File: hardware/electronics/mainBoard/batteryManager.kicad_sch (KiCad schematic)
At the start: 37 parts, among them J27 S3B-XH-SM4-TB, J28 1726480102, Q6 BUK6D72-30EX, Q7 BUK6D72-30EX, U22 BQ76905

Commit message: assigned FPs
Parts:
- D20: footprint (none) -> lib_diodes:SOD123
- J27: footprint (none) -> lib_connectors:JST_XH_S3B-SM4-TB
- J28: footprint (none) -> lib_connectors:1726480102
- Q6, Q7: footprint (none) -> lib_ICs:UDFN6P65_200X200X65L30X25N
- U22: footprint (none) -> lib_ICs:QFN50P350X350X100-20
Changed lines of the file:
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@@
 			)
 		)
-		(property "Footprint" ""
+		(property "Footprint" "lib_ICs:UDFN6P65_200X200X65L30X25N"
 			(at 186.055 142.24 90)
 			(effects
@@
 			)
 		)
-		(property "Footprint" ""
+		(property "Footprint" "lib_connectors:1726480102"
 			(at 26.67 64.77 0)
 			(effects
@@
 			)
 		)
-		(property "Footprint" ""
+		(property "Footprint" "lib_ICs:UDFN6P65_200X200X65L30X25N"
 			(at 205.105 142.24 90)
 			(effects
@@
 			)
 		)
-		(property "Footprint" ""
+		(property "Footprint" "lib_connectors:JST_XH_S3B-SM4-TB"
 			(at 35.56 30.48 0)
 			(effects
@@
 			)
 		)
-		(property "Footprint" ""
+		(property "Footprint" "lib_diodes:SOD123"
 			(at 224.79 133.35 90)
 			(effects
@@
 			)
 		)
-		(property "Footprint" ""
+		(property "Footprint" "lib_ICs:QFN50P350X350X100-20"
 			(at 154.94 99.06 0)
 			(effects

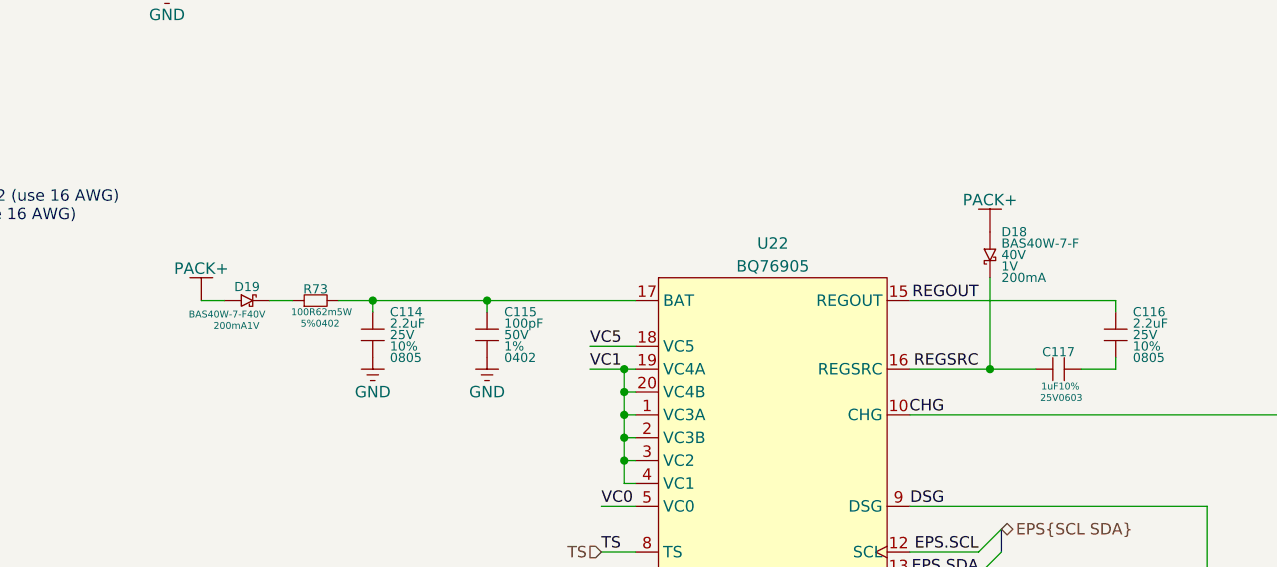
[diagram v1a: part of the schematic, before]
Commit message: added footprints to symbols
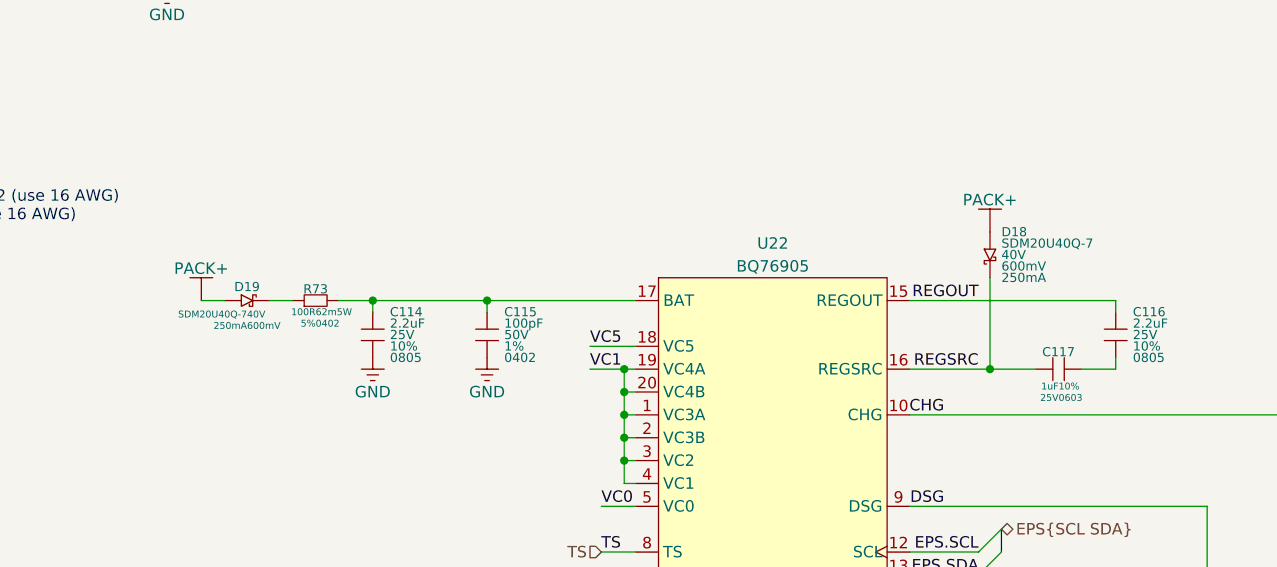
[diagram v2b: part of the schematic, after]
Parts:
- D18, D19: value BAS40W-7-F -> SDM20U40Q-7; footprint (none) -> lib_diodes:SOD523; Current 200mA -> 250mA; DKPN BAS40W-FDICT-ND -> 31-SDM20U40Q-7CT-ND; Forward Voltage 1V -> 600mV; MPN BAS40W-7-F -> SDM20U40Q-7
- R77: footprint (none) -> lib_passives:WSR4527
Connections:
- net PACK+: now also D18.2, D19.2; no longer D18.1, D19.1
- net REGSRC: now also D18.1; no longer D18.2
- net at R73.1: now also D19.1; no longer D19.2
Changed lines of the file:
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@@
 			)
 		)
-		(property "Footprint" ""
+		(property "Footprint" "lib_passives:WSR4527"
 			(at 88.9 121.92 0)
 			(effects
@@
 			)
 		)
-		(property "Value" "BAS40W-7-F"
+		(property "Value" "SDM20U40Q-7"
 			(at 165.1 81.28 0)
 			(do_not_autoplace yes)
@@
 			)
 		)
-		(property "Footprint" ""
+		(property "Footprint" "lib_diodes:SOD523"
 			(at 163.83 82.55 90)
 			(effects
@@
 			)
 		)
-		(property "Datasheet" "datasheets/Diodes-Incorporated-BAS40W_-04_-05_-06.pdf"
+		(property "Datasheet" "datasheets/Diodes-Incorporated-SDM20U40Q.pdf"
 			(at 163.83 82.55 90)
 			(effects
@@
 			)
 		)
-		(property "Description" "DIODE SCHOTTKY 40V 200MA SOT323"
+		(property "Description" "DIODE SCHOTTKY 40V 250MA SOD523"
 			(at 163.83 82.55 90)
 			(effects
@@
 			)
 		)
-		(property "MPN" "BAS40W-7-F"
+		(property "MPN" "SDM20U40Q-7"
 			(at 163.83 82.55 90)
 			(effects
@@
 			)
 		)
-		(property "DKPN" "BAS40W-FDICT-ND"
+		(property "DKPN" "31-SDM20U40Q-7CT-ND"
 			(at 163.83 82.55 90)
 			(effects
@@
 			)
 		)
-		(property "Forward Voltage" "1V"
+		(property "Forward Voltage" "600mV"
 			(at 165.1 83.82 0)
 			(do_not_autoplace yes)
@@
 			)
 		)
-		(property "Current" "200mA"
+		(property "Current" "250mA"
 			(at 165.1 85.09 0)
 			(do_not_autoplace yes)
@@
 			)
 		)
-		(property "Value" "BAS40W-7-F"
+		(property "Value" "SDM20U40Q-7"
 			(at 81.28 89.154 0)
 			(do_not_autoplace yes)
@@
 			)
 		)
-		(property "Footprint" ""
+		(property "Footprint" "lib_diodes:SOD523"
 			(at 81.28 87.63 0)
 			(effects
@@
 			)
 		)
-		(property "Datasheet" "datasheets/Diodes-Incorporated-BAS40W_-04_-05_-06.pdf"
+		(property "Datasheet" "datasheets/Diodes-Incorporated-SDM20U40Q.pdf"
 			(at 81.28 87.63 0)
 			(effects
@@
 			)
 		)
-		(property "Description" "DIODE SCHOTTKY 40V 200MA SOT323"
+		(property "Description" "DIODE SCHOTTKY 40V 250MA SOD523"
 			(at 81.28 87.63 0)
 			(effects
@@
 			)
 		)
-		(property "MPN" "BAS40W-7-F"
+		(property "MPN" "SDM20U40Q-7"
 			(at 81.28 87.63 0)
 			(effects
@@
 			)
 		)
-		(property "DKPN" "BAS40W-FDICT-ND"
+		(property "DKPN" "31-SDM20U40Q-7CT-ND"
 			(at 81.28 87.63 0)
 			(effects
@@
 			)
 		)
-		(property "Forward Voltage" "1V"
+		(property "Forward Voltage" "600mV"
 			(at 81.28 90.424 0)
 			(do_not_autoplace yes)
@@
 			)
 		)
-		(property "Current" "200mA"
+		(property "Current" "250mA"
 			(at 81.28 90.424 0)
 			(do_not_autoplace yes)

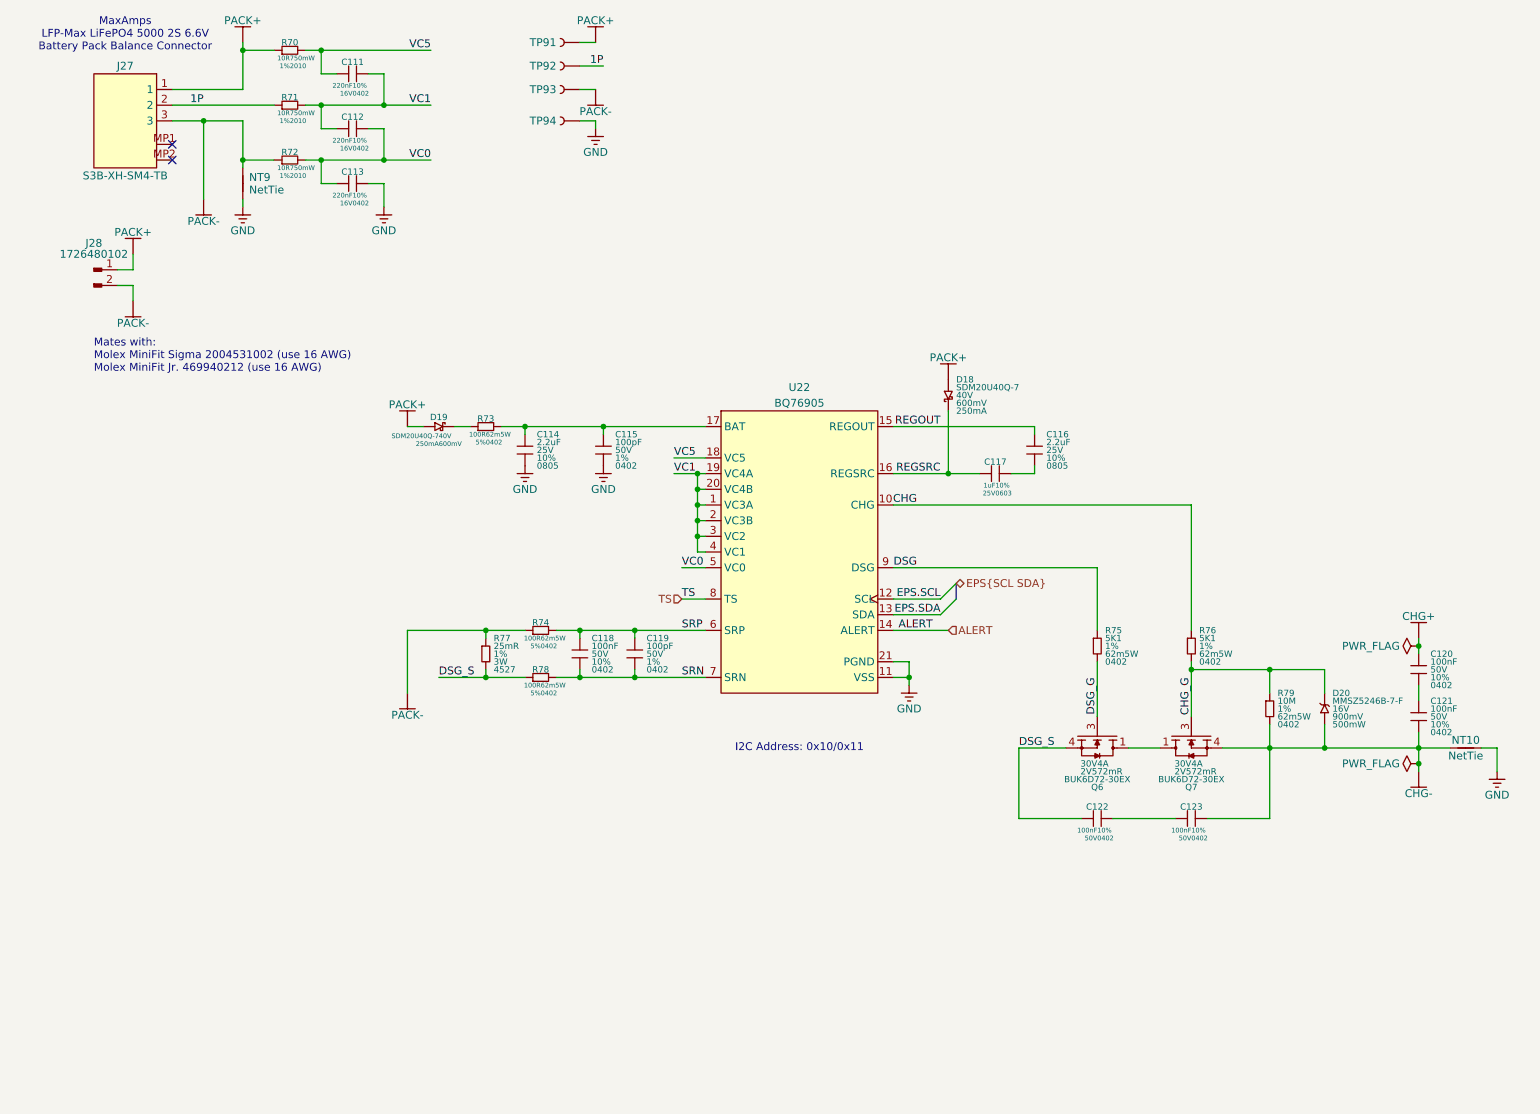
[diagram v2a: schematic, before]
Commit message: assigned footprints
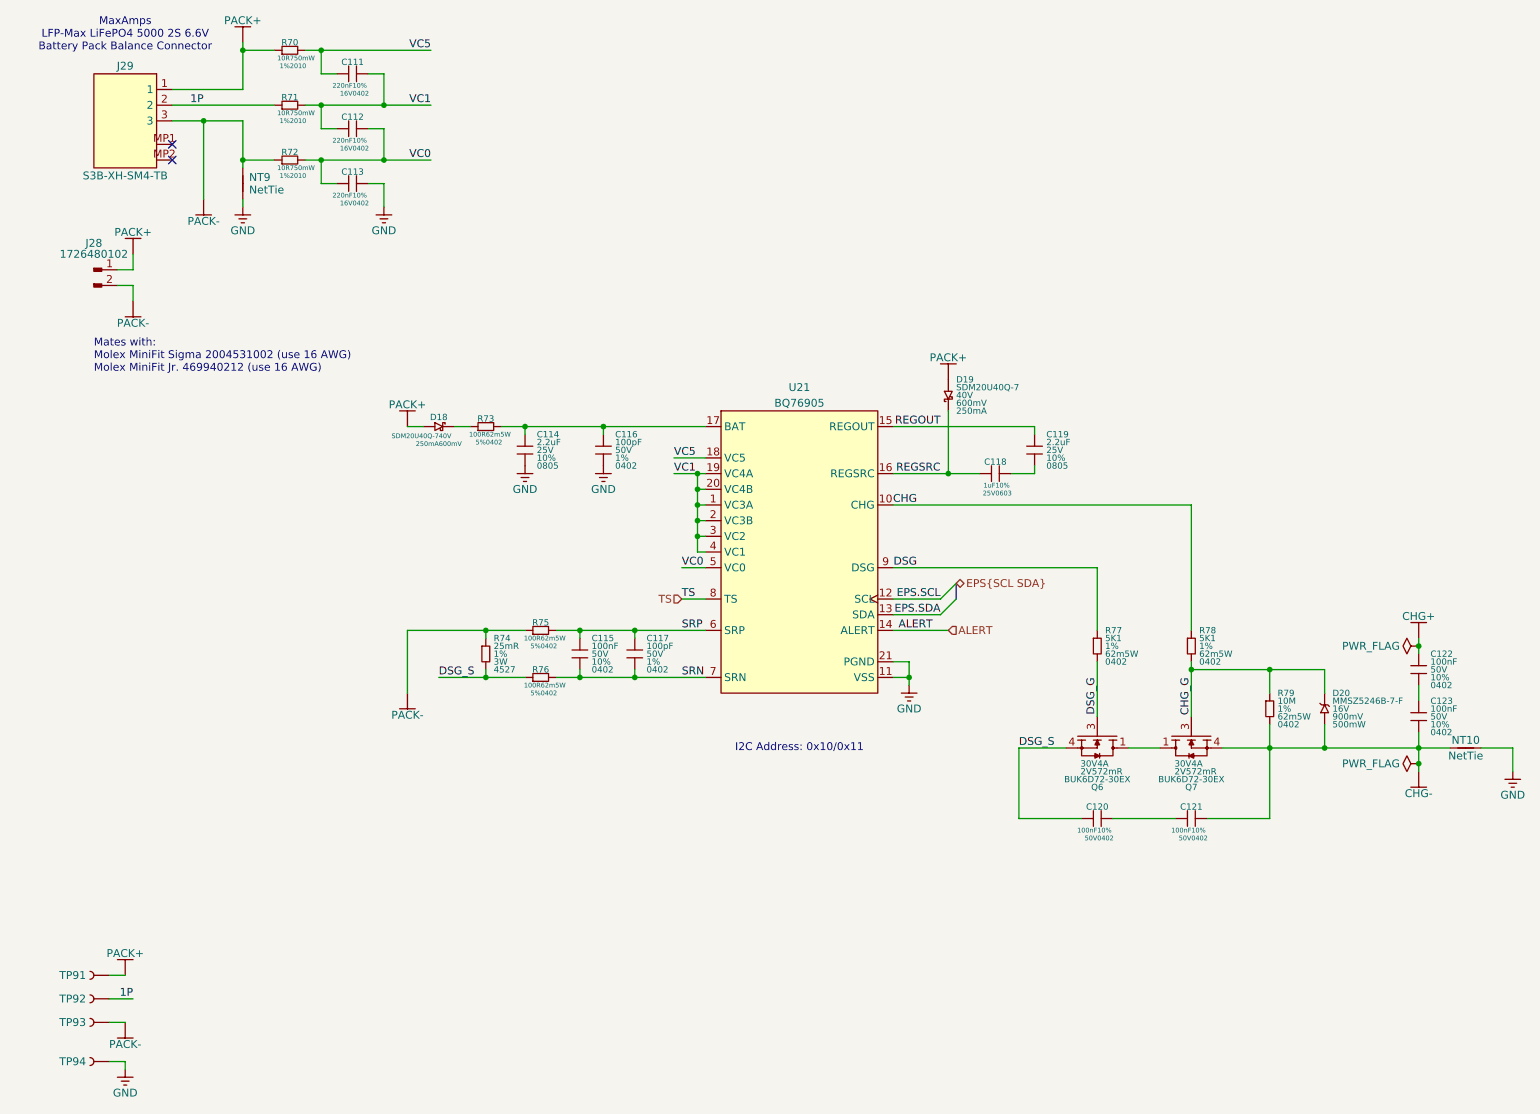
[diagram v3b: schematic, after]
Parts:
- C111, C112, C113: footprint (none) -> lib_passives:GCM0402
- C114: footprint (none) -> lib_passives:GCM0805
- C115: renamed from C118; footprint (none) -> lib_passives:GCM0402
- C116: renamed from C115; footprint (none) -> lib_passives:GCM0402
- C117: renamed from C119; footprint (none) -> lib_passives:GCM0402
- C118: renamed from C117; footprint (none) -> lib_passives:GRT0603
- C119: renamed from C116; footprint (none) -> lib_passives:GCM0805
- C120: renamed from C122; footprint (none) -> lib_passives:GCM0402
- C121: renamed from C123; footprint (none) -> lib_passives:GCM0402
- C122: renamed from C120; footprint (none) -> lib_passives:GCM0402
- C123: renamed from C121; footprint (none) -> lib_passives:GCM0402
- NT10, NT9: footprint (none) -> lib_misc:NetTie-2_SMD_Pad2.0mm
- R70, R71, R72: footprint (none) -> lib_passives:CRCW2010
- R73, R79: footprint (none) -> lib_passives:CRCW0402
- R75: renamed from R74; footprint (none) -> lib_passives:CRCW0402
- R76: renamed from R78; footprint (none) -> lib_passives:CRCW0402
- R77: renamed from R75; footprint (none) -> lib_passives:CRCW0402
- R78: renamed from R76; footprint (none) -> lib_passives:CRCW0402
- TP91, TP92: footprint (none) -> lib_misc:TP_2mm
- TP93, TP94: footprint (none) -> lib_misc:TP_RCW
- renumbered D19 to D18, D18 to D19, J27 to J29, R77 to R74, U22 to U21
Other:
- moved on the sheet: TP91, TP92, TP93, TP94

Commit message: updated ref designators
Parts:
- renumbered C116 to C115, C119 to C116, C118 to C117, C115 to C118, C117 to C119, C122 to C120, C123 to C121, C120 to C122, C121 to C123, D19 to D18, D18 to D19, J29 to J28, J28 to J29, R70 to R73, R71 to R74, R72 to R75, R73 to R76, R75 to R77, R77 to R78, R78 to R79, R74 to R80, R76 to R81, R79 to R82

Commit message: fixed sch
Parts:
- added NT10: NetTie, lib_misc:NetTie-2_SMD_Pad2.0mm, symbol lib_sch:NetTie
- R80: footprint lib_passives:WSR4527 -> lib_passives:CRCW2512-HP; DKPN WSRB-.025CT-ND -> WSLH-.04CT-ND; MPN WSR3R0250FEA -> WSL2512R0400FEA18; Package 4527 -> 2512; Power Rating 3W -> 2W
- renumbered NT10 to NT11
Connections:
- net CHG+: now also NT10.1
- net PACK+: now also NT10.2
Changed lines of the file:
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@@
 	)
 	(junction
+		(at 240.03 121.92)
+		(diameter 0)
+		(color 0 0 0 0)
+	)
+	(junction
 		(at 240.03 142.24)
 		(diameter 0)
@@
 	(wire
 		(pts
+			(xy 250.19 121.92) (xy 254 121.92)
+		)
+		(stroke
+			(width 0)
+			(type default)
+		)
+	)
+	(wire
+		(pts
 			(xy 72.39 48.26) (xy 72.39 52.07)
 		)
@@
 	(wire
 		(pts
+			(xy 240.03 121.92) (xy 245.11 121.92)
+		)
+		(stroke
+			(width 0)
+			(type default)
+		)
+	)
+	(wire
+		(pts
 			(xy 123.19 107.95) (xy 123.19 105.41)
 		)
@@
 			)
 		)
-		(property "Footprint" "lib_passives:WSR4527"
+		(property "Footprint" "lib_passives:CRCW2512-HP"
 			(at 88.9 121.92 0)
 			(effects
@@
 			)
 		)
-		(property "Datasheet" "datasheets/Vishay-Dale-WSR.pdf"
+		(property "Datasheet" "datasheets/Vishay-Dale-WSLH.pdf"
 			(at 88.9 121.92 0)
 			(effects
@@
 			)
 		)
-		(property "Description" "RES 0.025 OHM 1% 3W 4527"
+		(property "Description" "RES 0.04 OHM 1% 2W 2512"
 			(at 88.9 124.46 0)
 			(effects
@@
 			)
 		)
-		(property "MPN" "WSR3R0250FEA"
+		(property "MPN" "WSL2512R0400FEA18"
 			(at 88.9 121.92 0)
 			(effects
@@
 			)
 		)
-		(property "DKPN" "WSRB-.025CT-ND"
+		(property "DKPN" "WSLH-.04CT-ND"
 			(at 88.9 124.46 0)
 			(effects
@@
 			)
 		)
-		(property "Power Rating" "3W"
+		(property "Power Rating" "2W"
 			(at 90.17 125.73 0)
 			(do_not_autoplace yes)
@@
 			)
 		)
-		(property "Package" "4527"
+		(property "Package" "2512"
 			(at 90.17 127 0)
 			(do_not_autoplace yes)
@@
 	)
 	(symbol
+		(lib_id "lib_sch:NetTie")
+		(at 247.65 121.92 0)
+		(unit 1)
+		(exclude_from_sim no)
+		(in_bom no)
+		(on_board yes)
+		(dnp no)
+		(property "Reference" "NT10"
+			(at 247.65 120.65 0)
+			(do_not_autoplace yes)
+			(effects
+				(font
+					(size 1.27 1.27)
+				)
+			)
+		)
+		(property "Value" "NetTie"
+			(at 247.65 123.19 0)
+			(do_not_autoplace yes)
+			(effects
+				(font
+					(size 1.27 1.27)
+				)
+			)
+		)
+		(property "Footprint" "lib_misc:NetTie-2_SMD_Pad2.0mm"
+			(at 247.65 121.92 0)
+			(effects
+				(font
+					(size 1.27 1.27)
+				)
+				(hide yes)
+			)
+		)
+		(property "Datasheet" ""
+			(at 247.65 121.92 0)
+			(effects
+				(font
+					(size 1.27 1.27)
+				)
+				(hide yes)
+			)
+		)
+		(property "Description" "Net tie, 2 pins"
+			(at 247.65 121.92 0)
+			(effects
+				(font
+					(size 1.27 1.27)
+				)
+				(hide yes)
+			)
+		)
+		(pin "2"
+		)
+		(pin "1"
+		)
+		(instances
+			(project "mainBoard"
+				(path "/be16e32f-2ccf-4272-9ec7-94d5fe7a55e0/33ed3f59-5a0e-4fda-9238-d9f0ec67772d/972b2904-bf02-4c24-b7a7-11ba204fcc53"
+					(reference "NT10")
+					(unit 1)
+				)
+			)
+		)
+	)
+	(symbol
 		(lib_id "lib_sch:C_horizontal")
 		(at 67.31 30.48 0)
@@
 		(on_board yes)
 		(dnp no)
-		(property "Reference" "NT10"
+		(property "Reference" "NT11"
 			(at 247.65 138.43 0)
 			(do_not_autoplace yes)
@@
 			(project "mainBoard"
 				(path "/be16e32f-2ccf-4272-9ec7-94d5fe7a55e0/33ed3f59-5a0e-4fda-9238-d9f0ec67772d/972b2904-bf02-4c24-b7a7-11ba204fcc53"
-					(reference "NT10")
+					(reference "NT11")
 					(unit 1)
 				)
@@
 					(unit 1)
 				)
+			)
+		)
+	)
+	(symbol
+		(lib_id "lib_pwr:PACK+")
+		(at 254 121.92 0)
+		(unit 1)
+		(exclude_from_sim no)
+		(in_bom yes)
+		(on_board yes)
+		(dnp no)
+		(fields_autoplaced yes)
+		(property "Reference" "#PWR0306"
+			(at 254 121.92 0)
+			(effects
+				(font
+					(size 1.27 1.27)
+				)
+				(hide yes)
+			)
+		)
+		(property "Value" "PACK+"
+			(at 254 118.364 0)
+			(do_not_autoplace yes)
+			(effects
+				(font
+					(size 1.27 1.27)
+				)
+			)
+		)
+		(property "Footprint" ""
+			(at 254 121.92 0)
+			(effects
+				(font
+					(size 1.27 1.27)
+				)
+				(hide yes)
+			)
+		)
+		(property "Datasheet" ""
+			(at 254 121.92 0)
+			(effects
+				(font
+					(size 1.27 1.27)
+				)
+				(hide yes)
+			)
+		)
+		(property "Description" ""
+			(at 254 121.92 0)
+			(effects
+				(font
+					(size 1.27 1.27)
+				)
+				(hide yes)
+			)
+		)
+		(pin "1"
+		)
+		(instances
+			(project ""
+				(path "/be16e32f-2ccf-4272-9ec7-94d5fe7a55e0/33ed3f59-5a0e-4fda-9238-d9f0ec67772d/972b2904-bf02-4c24-b7a7-11ba204fcc53"
+					(reference "#PWR0306")
+					(unit 1)
+				)

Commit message: minor changes
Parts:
- R80: footprint lib_passives:CRCW2512-HP -> lib_passives:WSL2512-HP
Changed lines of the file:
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@@
 			)
 		)
-		(property "Footprint" "lib_passives:CRCW2512-HP"
+		(property "Footprint" "lib_passives:WSL2512-HP"
 			(at 88.9 121.92 0)
 			(effects

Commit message: redefined symbol refs
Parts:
- NT11: footprint lib_misc:NetTie-2_SMD_Pad2.0mm -> lib_misc:NetTie-2_SMD_Pad0.75mm
- renumbered C111 to C112, C112 to C113, C113 to C114, C114 to C115, C115 to C116, C116 to C117, C117 to C118, C118 to C119, C119 to C120, C120 to C121, C121 to C122, C122 to C123, C123 to C124, D18 to D16, D19 to D17, D20 to D18, R73 to R67, R74 to R68, R75 to R69, R76 to R70, R77 to R71, R78 to R72, R79 to R73, R80 to R74, R81 to R75, R82 to R76
